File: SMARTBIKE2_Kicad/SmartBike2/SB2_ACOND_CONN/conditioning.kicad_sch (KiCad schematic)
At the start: 20 parts, among them IC1 ESP32-WROVER-B__8MB_, J7 Conn_01x04, SW1 SW_Boot, SW2 SW_Reset

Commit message: Fase 2 de 3 panel full
+ PCB Acondicionamiento y Módulos

~ Esquemático Luces
~ PCB 3 de 3, Luces
~ Panelización
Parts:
- added J3: Conn_02x03_Counter_Clockwise, Connector_PinHeader_2.54mm:PinHeader_2x03_P2.54mm_Vertical, symbol Connector_Generic:Conn_02x03_Counter_Clockwise
- renumbered C15 to C?, C17 to C?, C16 to C?, C14 to C?, D4 to D?, D3 to D?, IC1 to IC?, J7 to J?, R33 to R?, R32 to R?, R36 to R?, R27 to R?, R28 to R?, R34 to R?, R31 to R?, R30 to R?, R35 to R?, R29 to R?, SW1 to SW?, SW2 to SW?
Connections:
- net Ctr_Al is gone; now on net TX_SIM: IC?.5 (SENSOR_VN)
- net Ctr_Luces is gone; now on net RX_SIM: IC?.6 (IO34)
- net RX_SIM: no longer IC?.11 (IO26)
- net TX_SIM: no longer IC?.10 (IO25)
- net MP2: now reaches IC?.23 (IO15)
- net MP2: now also J3.2 (Pin_2)
- net MP3: now reaches IC?.24 (IO2)
- net MP3: now also J3.3 (Pin_3)
- net MP4: now reaches IC?.29 (IO5)
- net MP4: now also J3.4 (Pin_4)
- net MP5: now reaches IC?.30 (IO18)
- net MP5: now also J3.5 (Pin_5)
- net MP6: now reaches IC?.31 (IO19)
- net MP6: now also J3.6 (Pin_6)
- net NE_SIM: now reaches IC?.7 (IO35)
- net CtrAl: now reaches IC?.8 (IO32)
- net RstSIM renamed CtrSIM
- net ctrGPSAc renamed MP1
- net MP1: now also J3.1 (Pin_1)
- net ctrSIM renamed RST_SIM
- new net CtrGPSAc: IC?.10 (IO25)
- new net CtrLuces: IC?.11 (IO26)
- no-connect marks 28 -> 21

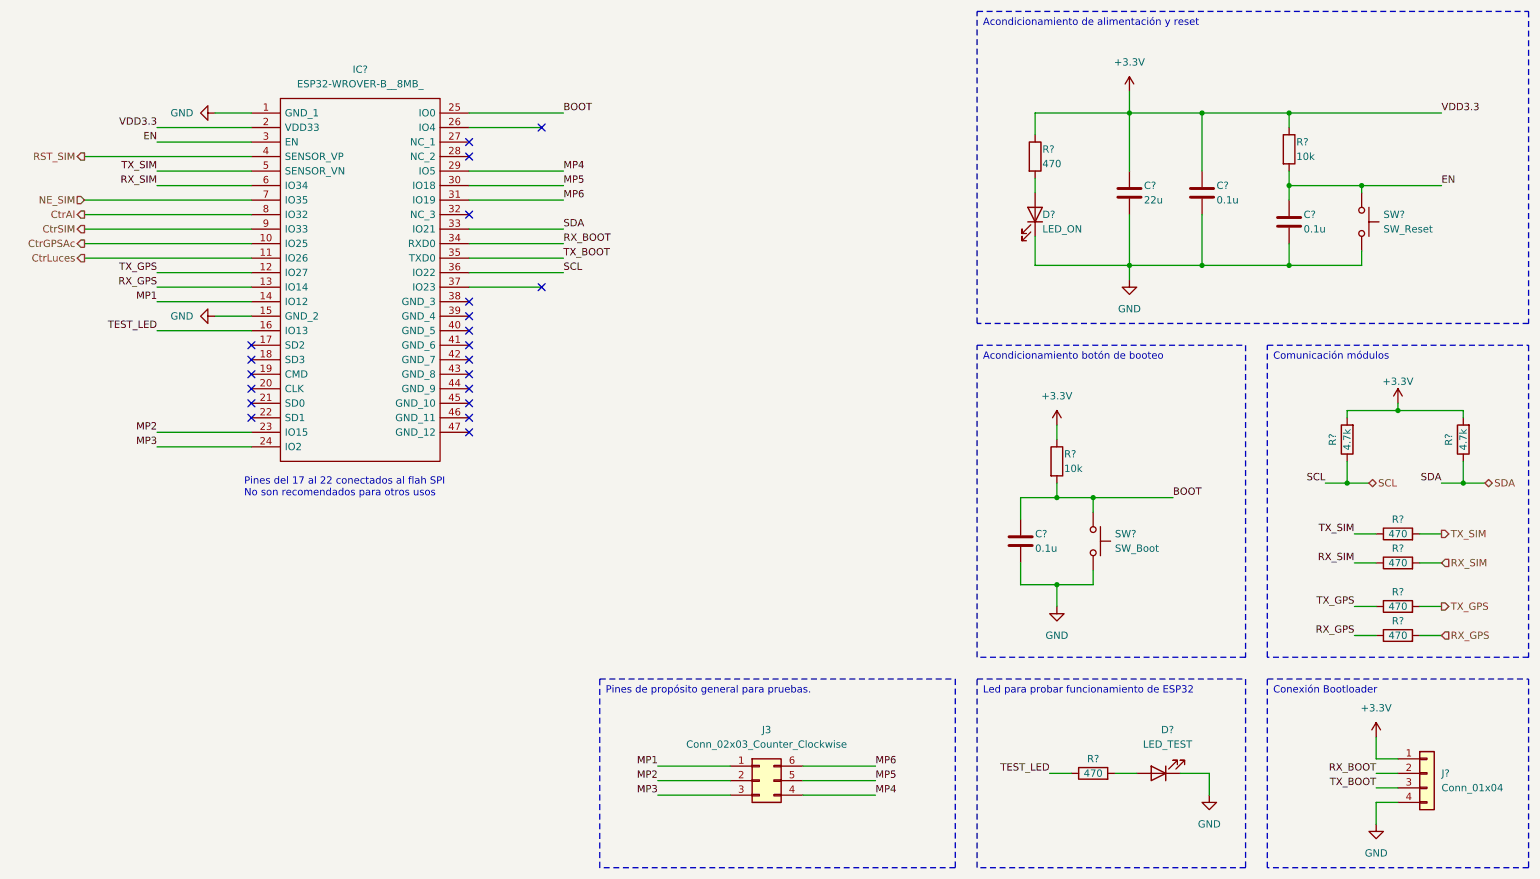
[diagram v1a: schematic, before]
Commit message: Impresión vías sin metalización
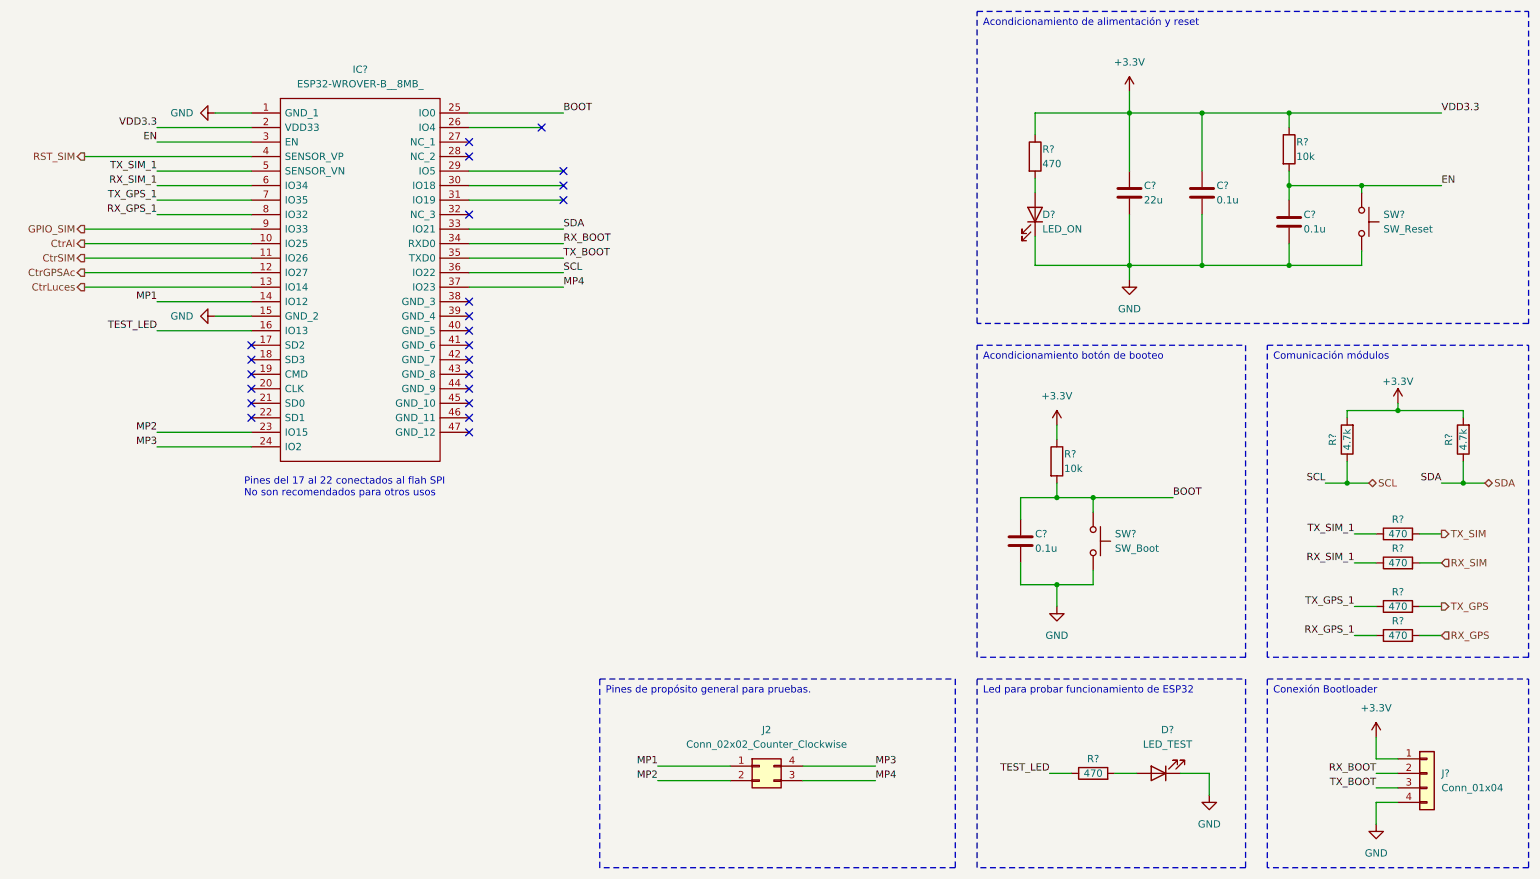
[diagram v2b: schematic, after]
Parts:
- removed J3: Conn_02x03_Counter_Clockwise, Connector_PinHeader_2.54mm:PinHeader_2x03_P2.54mm_Vertical, symbol Connector_Generic:Conn_02x03_Counter_Clockwise
- added J2: Conn_02x02_Counter_Clockwise, Connector_PinHeader_2.54mm:PinHeader_2x02_P2.54mm_Vertical, symbol Connector_Generic:Conn_02x02_Counter_Clockwise
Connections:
- net CtrAl: now also IC?.10 (IO25); no longer IC?.8 (IO32)
- net CtrGPSAc: now also IC?.12 (IO27); no longer IC?.10 (IO25)
- net CtrLuces: now also IC?.13 (IO14); no longer IC?.11 (IO26)
- net CtrSIM: now also IC?.11 (IO26); no longer IC?.9 (IO33)
- net MP1: now also J2.1 (Pin_1)
- net MP2: now also J2.2 (Pin_2)
- net MP3: now also J2.4 (Pin_4)
- net MP4: now also IC?.37 (IO23), J2.3 (Pin_3); no longer IC?.29 (IO5)
- net RX_GPS: no longer IC?.13 (IO14), R?.1
- net RX_SIM: no longer IC?.6 (IO34), R?.1
- net TX_GPS: no longer IC?.12 (IO27), R?.1
- net TX_SIM: no longer IC?.5 (SENSOR_VN), R?.1
- net MP5: no longer names the net of IC?.30 (IO18)
- net MP6: no longer names the net of IC?.31 (IO19)
- net NE_SIM renamed TX_GPS_1
- net TX_GPS_1: now also R?.1
- new net GPIO_SIM: IC?.9 (IO33)
- new net RX_GPS_1: IC?.8 (IO32), R?.1
- new net RX_SIM_1: IC?.6 (IO34), R?.1
- new net TX_SIM_1: IC?.5 (SENSOR_VN), R?.1
- no-connect marks 21 -> 23
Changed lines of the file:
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@@
   (no_connect (at 95.25 71.12))
   (no_connect (at 95.25 40.64))
+  (no_connect (at 111.76 43.18))
   (no_connect (at 57.15 81.28))
-  (no_connect (at 107.95 63.5))
+  (no_connect (at 111.76 45.72))
   (no_connect (at 95.25 38.1))
   (no_connect (at 57.15 83.82))
+  (no_connect (at 111.76 48.26))
   (no_connect (at 95.25 50.8))
   (no_connect (at 57.15 76.2))
@@
     (stroke (width 0) (type default))
   )
+  (wire (pts (xy 27.94 60.96) (xy 57.15 60.96))
+    (stroke (width 0) (type default))
+  )
   (wire (pts (xy 223.52 59.69) (xy 238.76 59.69))
     (stroke (width 0) (type default))
@@
     (stroke (width 0) (type default))
   )
-  (wire (pts (xy 40.64 63.5) (xy 57.15 63.5))
+  (wire (pts (xy 27.94 63.5) (xy 57.15 63.5))
     (stroke (width 0) (type default))
   )
@@
     (stroke (width 0) (type default))
   )
-  (wire (pts (xy 95.25 63.5) (xy 107.95 63.5))
+  (wire (pts (xy 95.25 63.5) (xy 111.76 63.5))
     (stroke (width 0) (type default))
   )
@@
     (stroke (width 0) (type default))
   )
-  (wire (pts (xy 153.67 152.4) (xy 166.37 152.4))
-    (stroke (width 0) (type default))
-  )
   (wire (pts (xy 238.76 43.18) (xy 238.76 45.72))
     (stroke (width 0) (type default))
@@
     (stroke (width 0) (type default))
   )
-  (wire (pts (xy 27.94 50.8) (xy 57.15 50.8))
+  (wire (pts (xy 40.64 50.8) (xy 57.15 50.8))
     (stroke (width 0) (type default))
   )
@@
     (stroke (width 0) (type default))
   )
-  (wire (pts (xy 27.94 48.26) (xy 57.15 48.26))
+  (wire (pts (xy 40.64 48.26) (xy 57.15 48.26))
     (stroke (width 0) (type default))
   )
@@
     (stroke (width 0) (type default))
   )
-  (wire (pts (xy 128.27 152.4) (xy 140.97 152.4))
-    (stroke (width 0) (type default))
-  )
   (wire (pts (xy 223.52 59.69) (xy 210.82 59.69))
     (stroke (width 0) (type default))
@@
   )
   (wire (pts (xy 224.79 148.59) (xy 224.79 152.4))
-    (stroke (width 0) (type default))
-  )
-  (wire (pts (xy 40.64 60.96) (xy 57.15 60.96))
     (stroke (width 0) (type default))
   )
@@
     (effects (font (size 1.27 1.27)) (justify right bottom))
   )
-  (label "MP3" (at 128.27 152.4 180) (fields_autoplaced)
-    (effects (font (size 1.27 1.27)) (justify right bottom))
-  )
   (label "SCL" (at 245.11 97.79 180) (fields_autoplaced)
     (effects (font (size 1.27 1.27)) (justify right bottom))
-  )
-  (label "MP6" (at 111.76 48.26 0) (fields_autoplaced)
-    (effects (font (size 1.27 1.27)) (justify left bottom))
   )
   (label "TX_BOOT" (at 111.76 58.42 0) (fields_autoplaced)
@@
     (effects (font (size 1.27 1.27)) (justify left bottom))
   )
-  (label "TX_GPS" (at 40.64 60.96 180) (fields_autoplaced)
+  (label "TX_GPS_1" (at 40.64 48.26 180) (fields_autoplaced)
     (effects (font (size 1.27 1.27)) (justify right bottom))
   )
   (label "RX_BOOT" (at 254 148.59 180) (fields_autoplaced)
     (effects (font (size 1.27 1.27)) (justify right bottom))
-  )
-  (label "MP4" (at 166.37 152.4 0) (fields_autoplaced)
-    (effects (font (size 1.27 1.27)) (justify left bottom))
   )
   (label "MP3" (at 40.64 91.44 180) (fields_autoplaced)
@@
     (effects (font (size 1.27 1.27)) (justify right bottom))
   )
-  (label "TX_SIM" (at 250.19 106.68 180) (fields_autoplaced)
+  (label "TX_SIM_1" (at 250.19 106.68 180) (fields_autoplaced)
     (effects (font (size 1.27 1.27)) (justify right bottom))
   )
@@
     (effects (font (size 1.27 1.27)) (justify right bottom))
   )
-  (label "RX_SIM" (at 250.19 111.76 180) (fields_autoplaced)
+  (label "RX_SIM_1" (at 250.19 111.76 180) (fields_autoplaced)
     (effects (font (size 1.27 1.27)) (justify right bottom))
   )
@@
     (effects (font (size 1.27 1.27)) (justify right bottom))
   )
-  (label "MP5" (at 166.37 149.86 0) (fields_autoplaced)
+  (label "MP4" (at 166.37 149.86 0) (fields_autoplaced)
     (effects (font (size 1.27 1.27)) (justify left bottom))
   )
@@
     (effects (font (size 1.27 1.27)) (justify left bottom))
   )
-  (label "RX_SIM" (at 40.64 45.72 180) (fields_autoplaced)
-    (effects (font (size 1.27 1.27)) (justify right bottom))
-  )
-  (label "TX_SIM" (at 40.64 43.18 180) (fields_autoplaced)
+  (label "RX_SIM_1" (at 40.64 45.72 180) (fields_autoplaced)
+    (effects (font (size 1.27 1.27)) (justify right bottom))
+  )
+  (label "TX_SIM_1" (at 40.64 43.18 180) (fields_autoplaced)
     (effects (font (size 1.27 1.27)) (justify right bottom))
   )
@@
     (effects (font (size 1.27 1.27)) (justify right bottom))
   )
-  (label "RX_GPS" (at 250.19 124.46 180) (fields_autoplaced)
-    (effects (font (size 1.27 1.27)) (justify right bottom))
-  )
-  (label "TX_GPS" (at 250.19 119.38 180) (fields_autoplaced)
+  (label "RX_GPS_1" (at 250.19 124.46 180) (fields_autoplaced)
+    (effects (font (size 1.27 1.27)) (justify right bottom))
+  )
+  (label "TX_GPS_1" (at 250.19 119.38 180) (fields_autoplaced)
     (effects (font (size 1.27 1.27)) (justify right bottom))
   )
@@
     (effects (font (size 1.27 1.27)) (justify left bottom))
   )
-  (label "MP6" (at 166.37 147.32 0) (fields_autoplaced)
+  (label "MP3" (at 166.37 147.32 0) (fields_autoplaced)
     (effects (font (size 1.27 1.27)) (justify left bottom))
   )
-  (label "MP5" (at 111.76 45.72 0) (fields_autoplaced)
-    (effects (font (size 1.27 1.27)) (justify left bottom))
-  )
   (label "VDD3.3" (at 40.64 35.56 180) (fields_autoplaced)
     (effects (font (size 1.27 1.27)) (justify right bottom))
@@
     (effects (font (size 1.27 1.27)) (justify right bottom))
   )
-  (label "MP4" (at 111.76 43.18 0) (fields_autoplaced)
+  (label "MP4" (at 111.76 63.5 0) (fields_autoplaced)
     (effects (font (size 1.27 1.27)) (justify left bottom))
   )
@@
     (effects (font (size 1.27 1.27)) (justify left bottom))
   )
-  (label "RX_GPS" (at 40.64 63.5 180) (fields_autoplaced)
+  (label "RX_GPS_1" (at 40.64 50.8 180) (fields_autoplaced)
     (effects (font (size 1.27 1.27)) (justify right bottom))
   )
@@
     (effects (font (size 1.27 1.27)) (justify left))
   )
-  (hierarchical_label "CtrAl" (shape output) (at 27.94 50.8 180) (fields_autoplaced)
+  (hierarchical_label "CtrAl" (shape output) (at 27.94 55.88 180) (fields_autoplaced)
     (effects (font (size 1.27 1.27)) (justify right))
   )
-  (hierarchical_label "NE_SIM" (shape input) (at 27.94 48.26 180) (fields_autoplaced)
+  (hierarchical_label "GPIO_SIM" (shape output) (at 27.94 53.34 180) (fields_autoplaced)
     (effects (font (size 1.27 1.27)) (justify right))
   )
@@
     (effects (font (size 1.27 1.27)) (justify left))
   )
-  (hierarchical_label "CtrLuces" (shape output) (at 27.94 58.42 180) (fields_autoplaced)
+  (hierarchical_label "CtrLuces" (shape output) (at 27.94 63.5 180) (fields_autoplaced)
     (effects (font (size 1.27 1.27)) (justify right))
   )
-  (hierarchical_label "CtrSIM" (shape output) (at 27.94 53.34 180) (fields_autoplaced)
+  (hierarchical_label "CtrSIM" (shape output) (at 27.94 58.42 180) (fields_autoplaced)
     (effects (font (size 1.27 1.27)) (justify right))
   )
@@
     (effects (font (size 1.27 1.27)) (justify left))
   )
-  (hierarchical_label "CtrGPSAc" (shape output) (at 27.94 55.88 180) (fields_autoplaced)
+  (hierarchical_label "CtrGPSAc" (shape output) (at 27.94 60.96 180) (fields_autoplaced)
     (effects (font (size 1.27 1.27)) (justify right))
   )
@@
         (path "/f851423c-110f-48a5-8b48-ed3566b6f957/9f7d6d51-72a6-4eae-b4d4-ee243c541bc7"
           (reference "#PWR05") (unit 1)
+        )
+      )
+    )
+  )
+  (symbol (lib_id "Connector_Generic:Conn_02x02_Counter_Clockwise") (at 146.05 147.32 0) (unit 1)
+    (in_bom yes) (on_board yes) (dnp no) (fields_autoplaced)
+    (property "Reference" "J2" (at 147.32 140.97 0)
+      (effects (font (size 1.27 1.27)))
+    )
+    (property "Value" "Conn_02x02_Counter_Clockwise" (at 147.32 143.51 0)
+      (effects (font (size 1.27 1.27)))
+    )
+    (property "Footprint" "Connector_PinHeader_2.54mm:PinHeader_2x02_P2.54mm_Vertical" (at 146.05 147.32 0)
+      (effects (font (size 1.27 1.27)) hide)
+    )
+    (property "Datasheet" "~" (at 146.05 147.32 0)
+      (effects (font (size 1.27 1.27)) hide)
+    )
+    (pin "2")
+    (pin "3")
+    (pin "4")
+    (pin "1")
+    (instances
+      (project "SB2_ACOND_CONN"
+        (path "/f851423c-110f-48a5-8b48-ed3566b6f957/9f7d6d51-72a6-4eae-b4d4-ee243c541bc7"
+          (reference "J2") (unit 1)
         )
       )
@@
       (project "SB2_ACOND_CONN"
         (path "/f851423c-110f-48a5-8b48-ed3566b6f957/9f7d6d51-72a6-4eae-b4d4-ee243c541bc7"
-          (reference "J4") (unit 1)
-        )
-      )
-    )
-  )
-  (symbol (lib_id "Connector_Generic:Conn_02x03_Counter_Clockwise") (at 146.05 149.86 0) (unit 1)
-    (in_bom yes) (on_board yes) (dnp no) (fields_autoplaced)
-    (property "Reference" "J3" (at 147.32 140.97 0)
-      (effects (font (size 1.27 1.27)))
-    )
-    (property "Value" "Conn_02x03_Counter_Clockwise" (at 147.32 143.51 0)
-      (effects (font (size 1.27 1.27)))
-    )
-    (property "Footprint" "Connector_PinHeader_2.54mm:PinHeader_2x03_P2.54mm_Vertical" (at 146.05 149.86 0)
-      (effects (font (size 1.27 1.27)) hide)
-    )
-    (property "Datasheet" "~" (at 146.05 149.86 0)
-      (effects (font (size 1.27 1.27)) hide)
-    )
-    (pin "2")
-    (pin "1")
-    (pin "5")
-    (pin "4")
-    (pin "6")
-    (pin "3")
-    (instances
-      (project "SB2_ACOND_CONN"
-        (path "/f851423c-110f-48a5-8b48-ed3566b6f957/9f7d6d51-72a6-4eae-b4d4-ee243c541bc7"
